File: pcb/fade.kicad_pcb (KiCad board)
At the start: 2 copper layers, 34.7 x 16.8 mm, 14 parts, among them CON1 AVR-ISP-6, CON2 USB-MINI-B, IC1 ATTINY85-P, P1 CONN_5

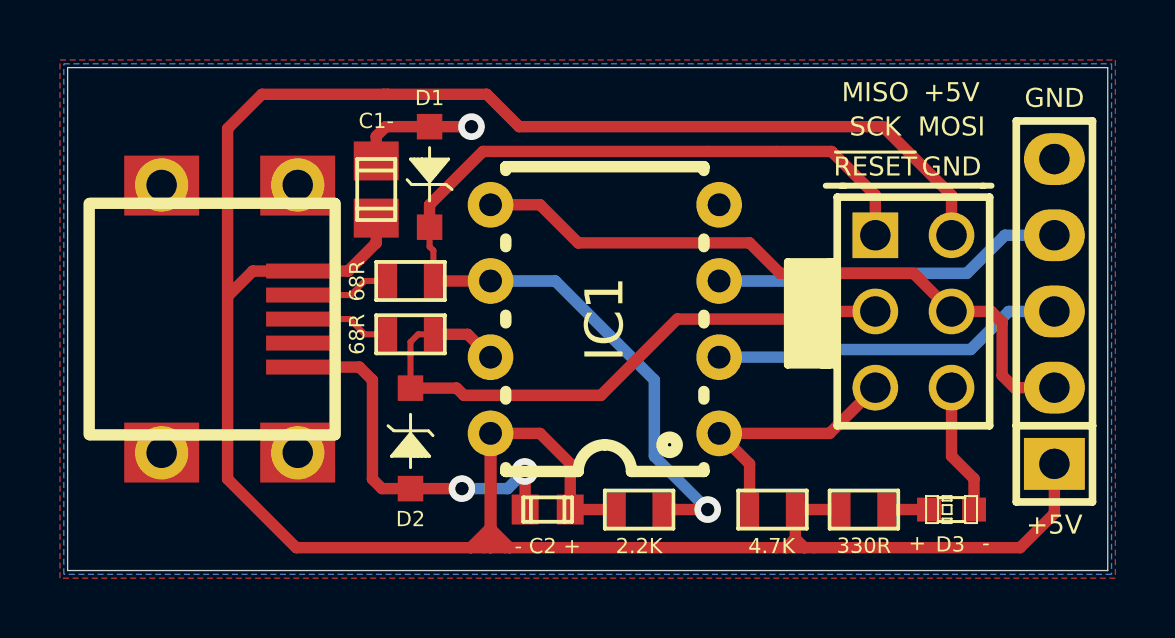
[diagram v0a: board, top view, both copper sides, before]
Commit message: Updated fade against KiCad 4.0.7
Note: DRC is broken, but this board's layout has not changed (it
should still be fabbable with a desktop PCB milling machine).
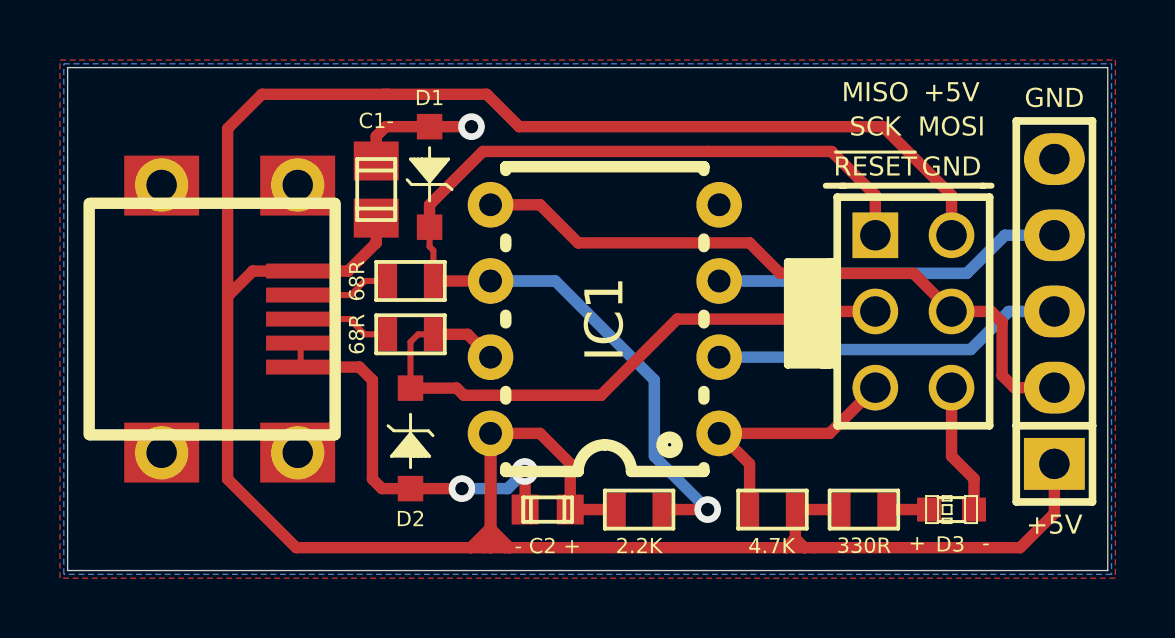
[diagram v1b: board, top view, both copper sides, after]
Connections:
- CON2 pad 4: Net-(CON2-Pad4) -> GND
- CON2 pad 6: Net-(CON2-Pad6) -> (no net)
- CON2 pad 7: Net-(CON2-Pad7) -> (no net)
- CON2 pad 8: Net-(CON2-Pad8) -> (no net)
- CON2 pad 9: Net-(CON2-Pad9) -> (no net)
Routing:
- net GND: track 21.1 -> 21.9 mm
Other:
- net class 1/100 removed
- net class 1/32 bit removed
- net class 1/64 bit removed
